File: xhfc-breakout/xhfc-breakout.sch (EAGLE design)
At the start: 2 parts, among them U1 XHFC-2SU

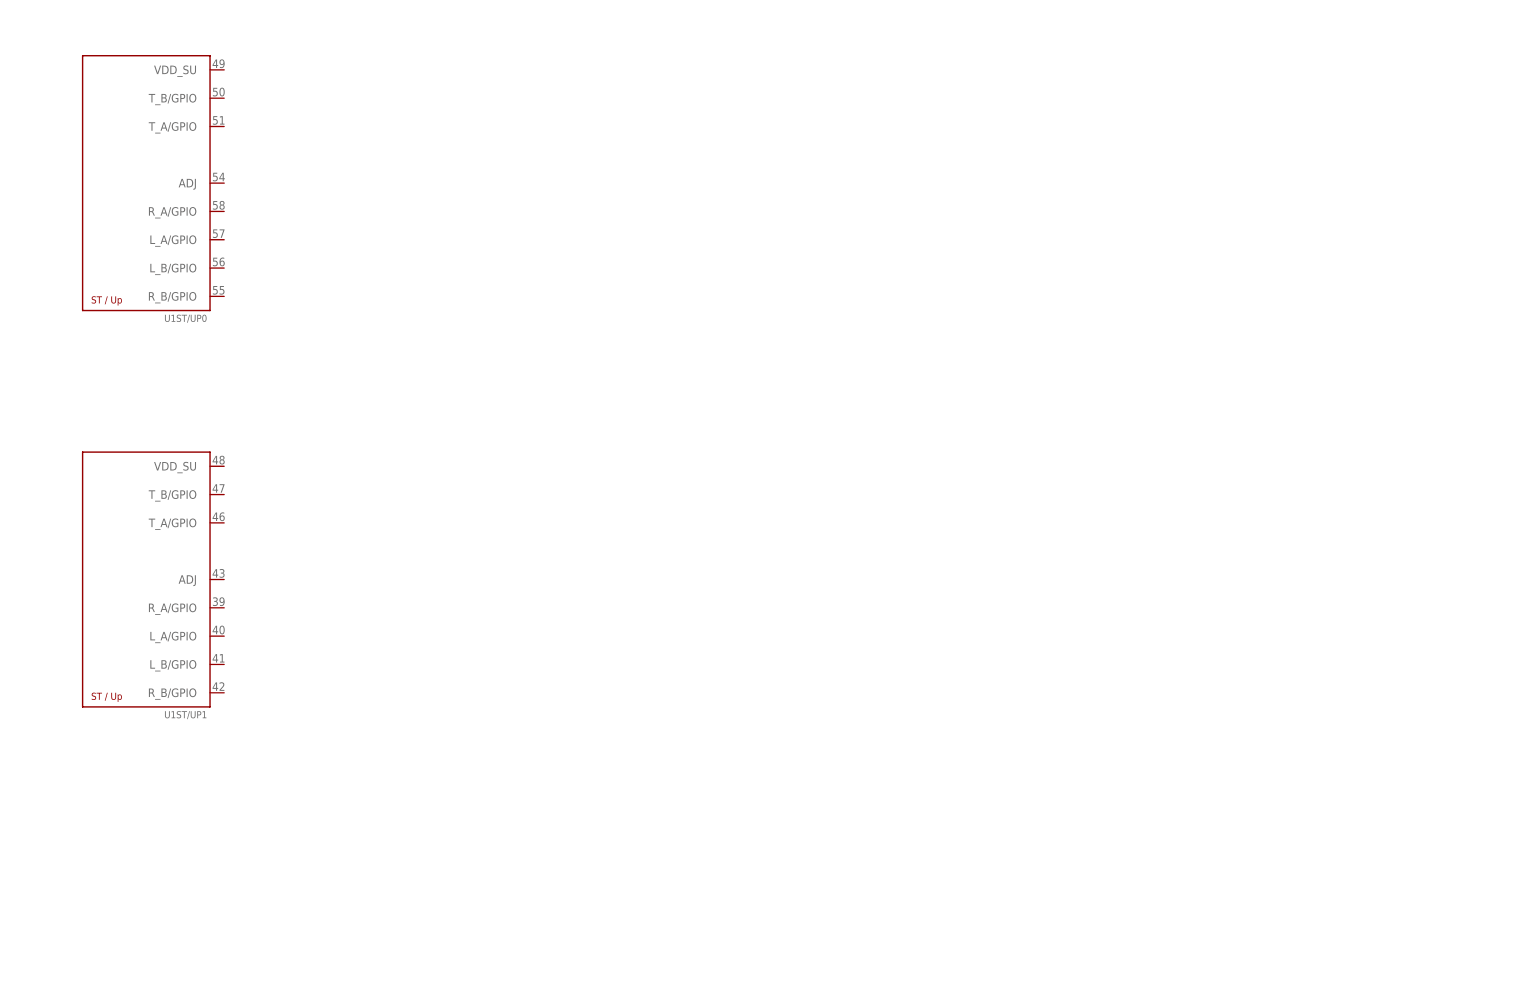
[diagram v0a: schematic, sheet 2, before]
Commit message: xhfc-breakout: Complete line interface from chip to RJ45
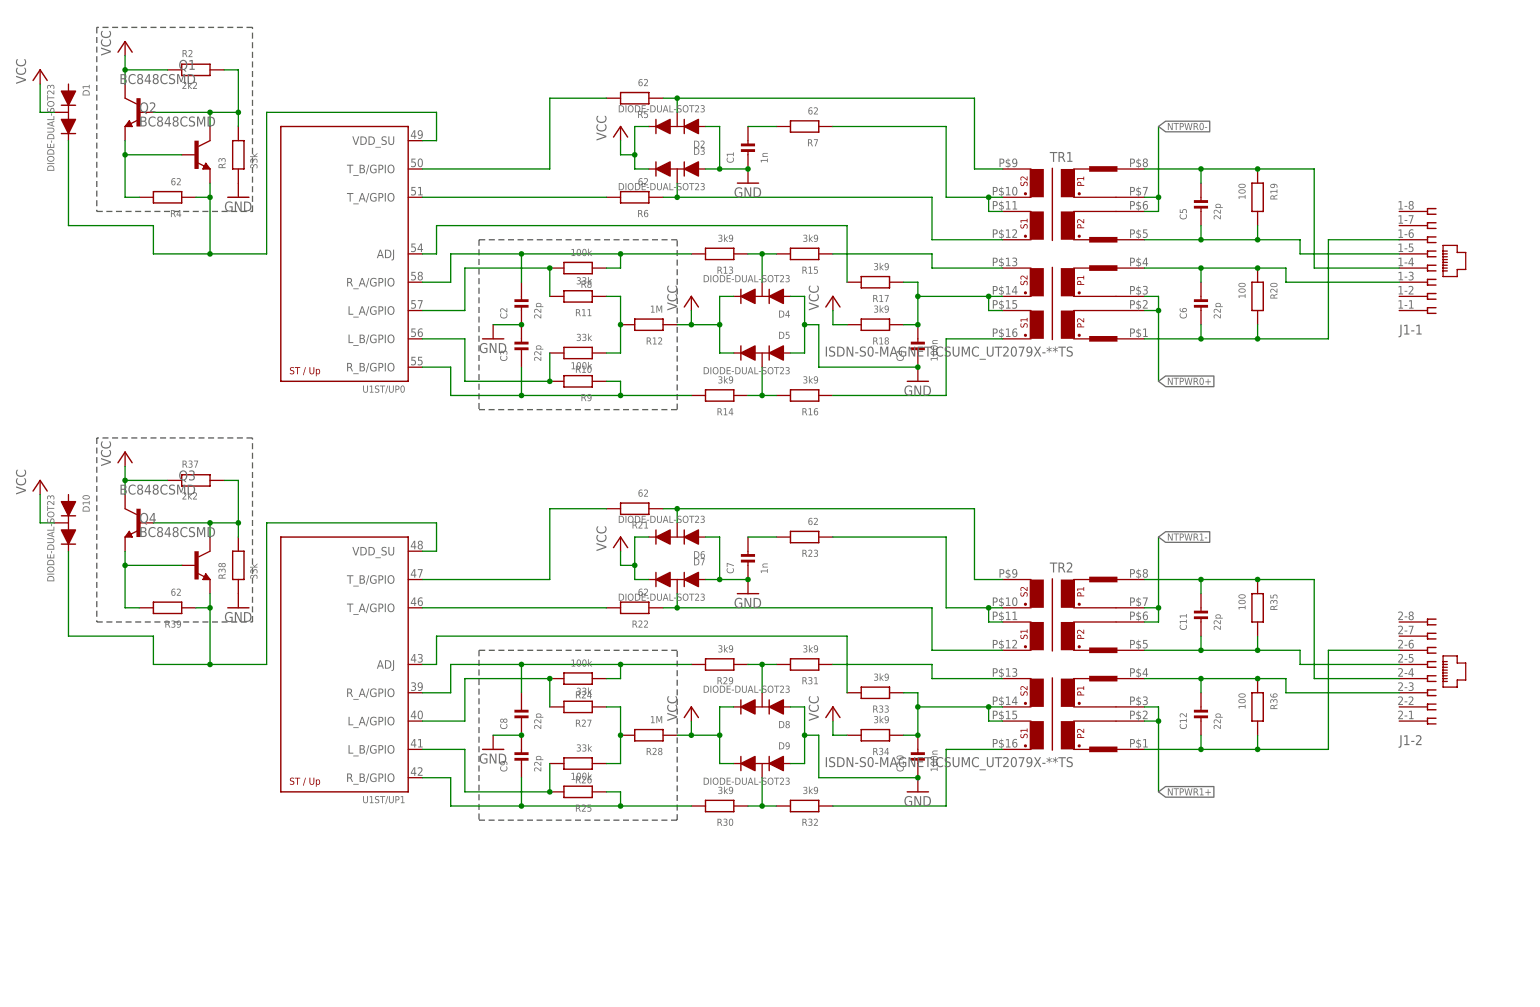
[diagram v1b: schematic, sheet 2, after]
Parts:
- added C1, C7: 1n, rc-sysmocom:CAP_CERAMIC_0603
- added C10, C4: 100n, rc-sysmocom:CAP_CERAMIC_0603
- added C11, C12, C2, C3, C5, C6, C8, C9: 22p, rc-sysmocom:CAP_CERAMIC_0603
- added D1, D10, D2, D3, D4, D5, D6, D7, D8, D9: DIODE-DUAL-SOT23, diodes-sysmocom:DIODE-DUAL-SOT23
- added J1: (no value), con-amp:557560-1
- added Q1, Q2, Q3, Q4: BC848CSMD, transistor-npn:BC848CSMD
- added R10, R11, R26, R27, R3, R38: 33k, rc-sysmocom:RESISTOR_0603
- added R12, R28: 1M, rc-sysmocom:RESISTOR_0603
- added R13, R14, R15, R16, R17, R18, R29, R30, R31, R32, R33, R34: 3k9, rc-sysmocom:RESISTOR_0603
- added R19, R20, R35, R36: 100, rc-sysmocom:RESISTOR_0603
- added R2, R37: 2k2, rc-sysmocom:RESISTOR_0603
- added R21, R22, R23, R39, R4, R5, R6, R7: 62, rc-sysmocom:RESISTOR_0603
- added R24, R25, R8, R9: 100k, rc-sysmocom:RESISTOR_0603
- added TR1, TR2: ISDN-S0-MAGNETICSUMC_UT2079X-**TS, isdn-magnetics:ISDN-S0-MAGNETICSUMC_UT2079X-**TS
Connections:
- new net N$1: Q1.B, Q2.C, R2.2, R3.2
- new net N$10: R7.1, TR1.10, TR1.11
- new net N$11: C3.1, R14.2, R9.1, U1ST/UP0.R_B/GPIO
- new net N$12: C2.2, R13.2, R8.1, U1ST/UP0.R_A/GPIO
- new net N$13: R11.2, R8.2, U1ST/UP0.L_A/GPIO
- new net N$14: R17.2, U1ST/UP0.ADJ
- new net N$15: R10.2, R9.2, U1ST/UP0.L_B/GPIO
- new net N$16: R10.1, R11.1, R12.2
- new net N$17: D6.M, R21.1, TR2.9
- new net N$18: C5.2, J1-1.4, R19.1, TR1.8
- new net N$19: D4.M, R13.1, R15.2
- new net N$2: R5.2, U1ST/UP0.T_B/GPIO
- new net N$20: D5.M, R14.1, R16.2
- new net N$21: C5.1, J1-1.5, R19.2, TR1.5
- new net N$22: R15.1, TR1.13
- new net N$23: R16.1, TR1.16
- new net N$24: C4.2, R17.1, R18.1, TR1.14, TR1.15
- new net N$25: C6.2, J1-1.3, R20.1, TR1.4
- new net N$26: C6.1, J1-1.6, R20.2, TR1.1
- new net N$27: D7.M, R22.1, TR2.12
- new net N$28: R21.2, U1ST/UP1.T_B/GPIO
- new net N$29: R22.2, U1ST/UP1.T_A/GPIO
- new net N$3: Q1.E, Q2.B, R4.2
- new net N$30: C7.2, R23.2
- new net N$31: R23.1, TR2.10, TR2.11
- new net N$32: R33.2, U1ST/UP1.ADJ
- new net N$33: C9.1, R25.1, R30.2, U1ST/UP1.R_B/GPIO
- new net N$34: C8.2, R24.1, R29.2, U1ST/UP1.R_A/GPIO
- new net N$35: R24.2, R27.2, U1ST/UP1.L_A/GPIO
- new net N$36: R25.2, R26.2, U1ST/UP1.L_B/GPIO
- new net N$37: R26.1, R27.1, R28.2
- new net N$38: D8.M, R29.1, R31.2
- new net N$39: D9.M, R30.1, R32.2
- new net N$4: D1.C, Q2.E, R4.1, U1ST/UP0.VDD_SU
- new net N$40: R31.1, TR2.13
- new net N$41: R32.1, TR2.16
- new net N$42: C10.2, R33.1, R34.1, TR2.14, TR2.15
- new net N$43: C11.2, J1-2.4, R35.1, TR2.8
- new net N$44: C11.1, J1-2.5, R35.2, TR2.5
- new net N$45: C12.2, J1-2.3, R36.1, TR2.4
- new net N$46: C12.1, J1-2.6, R36.2, TR2.1
- new net N$47: Q3.B, Q4.C, R37.2, R38.2
- new net N$48: Q3.E, Q4.B, R39.2
- new net N$49: D10.C, Q4.E, R39.1, U1ST/UP1.VDD_SU
- new net N$5: R6.2, U1ST/UP0.T_A/GPIO
- new net N$6: D2.M, R5.1, TR1.9
- new net N$7: D3.M, R6.1, TR1.12
- new net N$8: C1.1, C7.1, D2.A, D3.A, D6.A, D7.A
- new net N$9: C1.2, R7.2
- new net NTPWR0+: TR1.2, TR1.3
- new net NTPWR0-: TR1.6, TR1.7
- new net NTPWR1+: TR2.2, TR2.3
- new net NTPWR1-: TR2.6, TR2.7
- net GND: now also C10.1, C2.1, C3.2, C4.1, C8.1, C9.2, D4.A, D5.A, D8.A, D9.A, R3.1, R38.1
- net VCC: now also D1.M, D10.M, D2.C, D3.C, D4.C, D5.C, D6.C, D7.C, D8.C, D9.C, Q1.C, Q3.C, R12.1, R18.2, R2.1, R28.1, R34.2, R37.1
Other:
- moved on the sheet: U1ST/UP0, U1ST/UP1

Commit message: xhfc-breakout: Smash parts / align labels / better readability
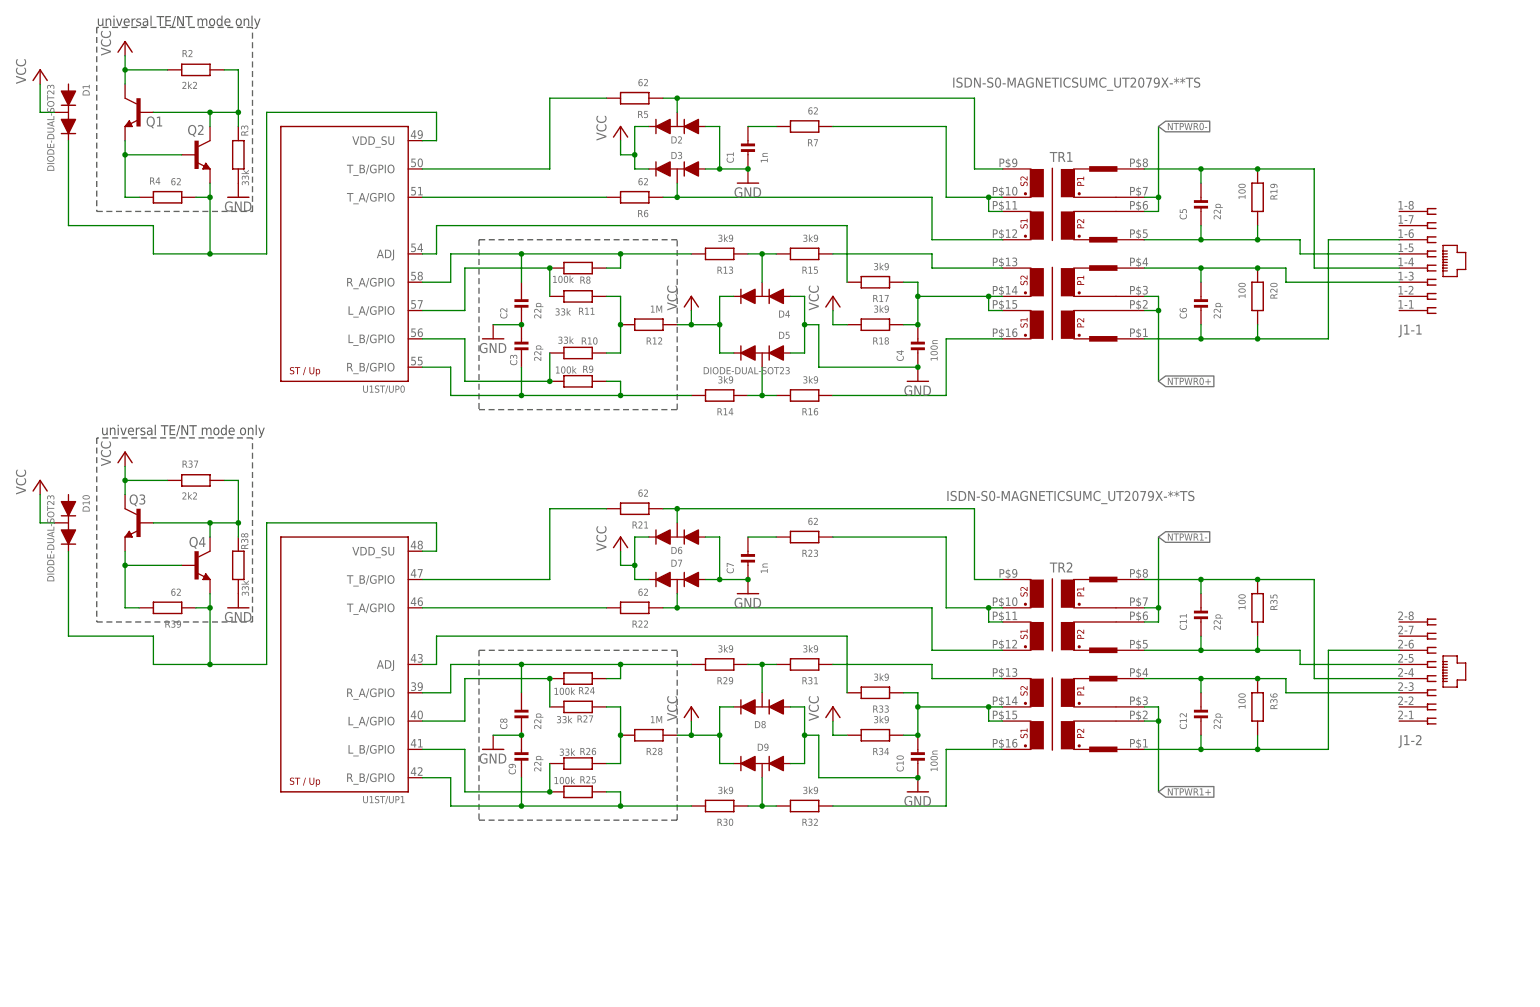
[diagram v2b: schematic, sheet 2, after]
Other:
- note added: "universal TE/NT mode only"

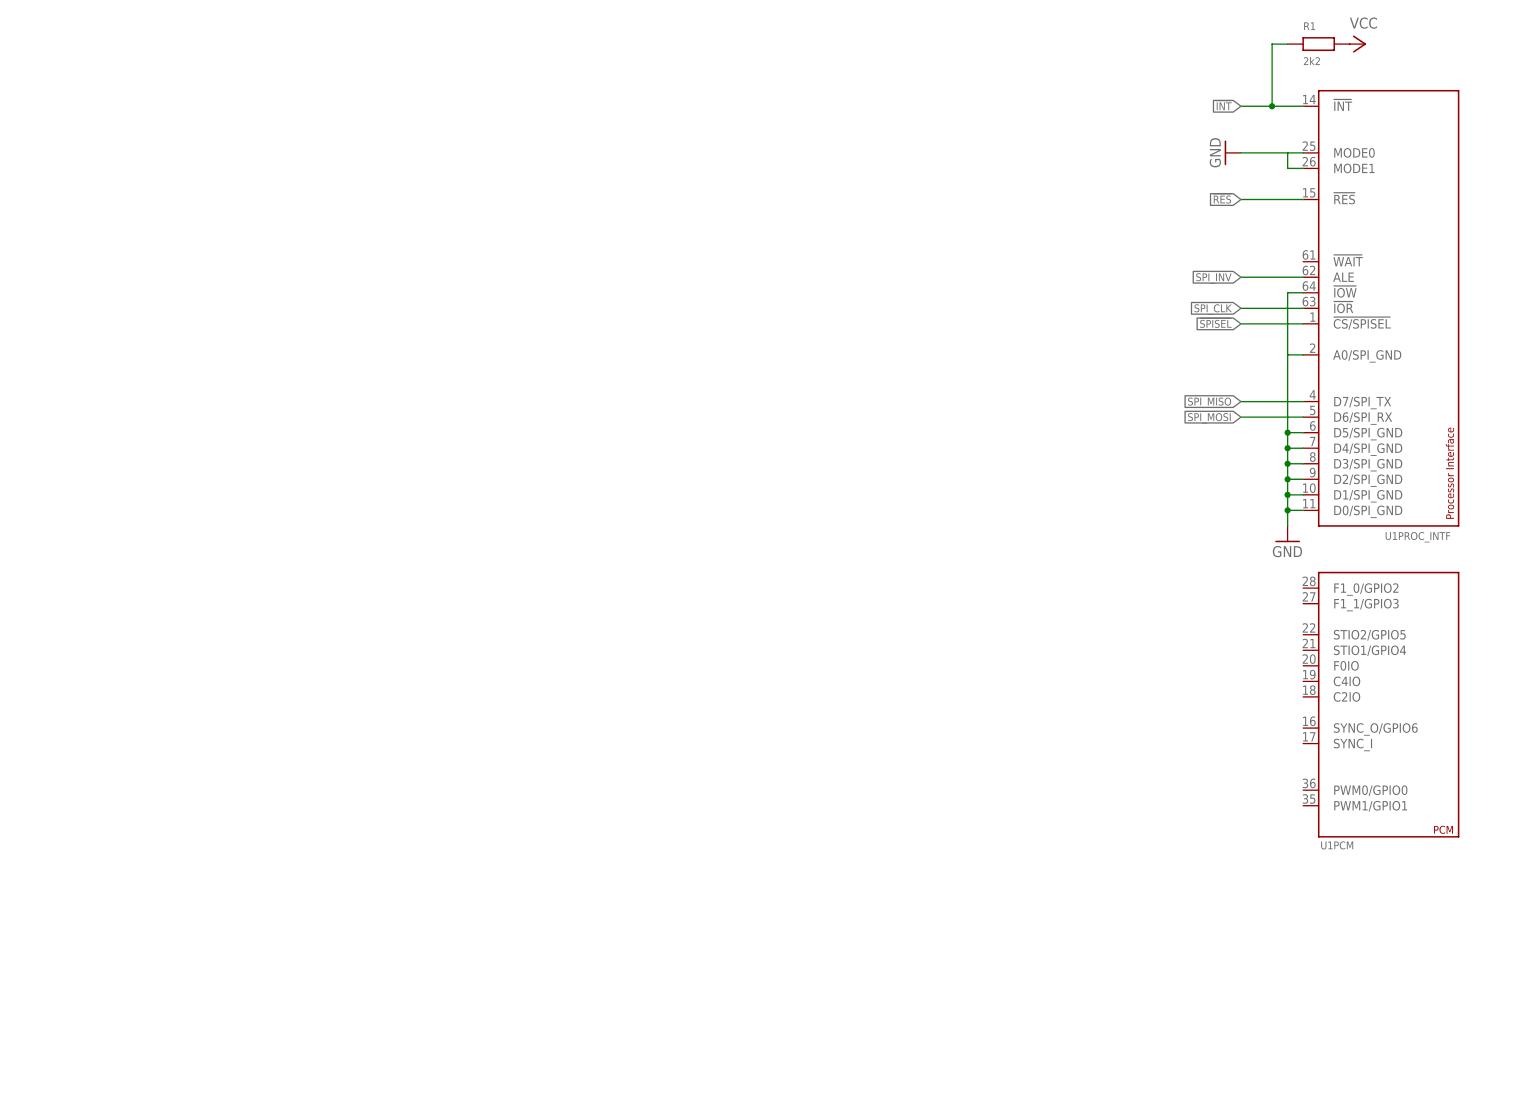
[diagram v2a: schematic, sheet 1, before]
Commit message: xhfc-breakout: partial PCB layout / component arrangement
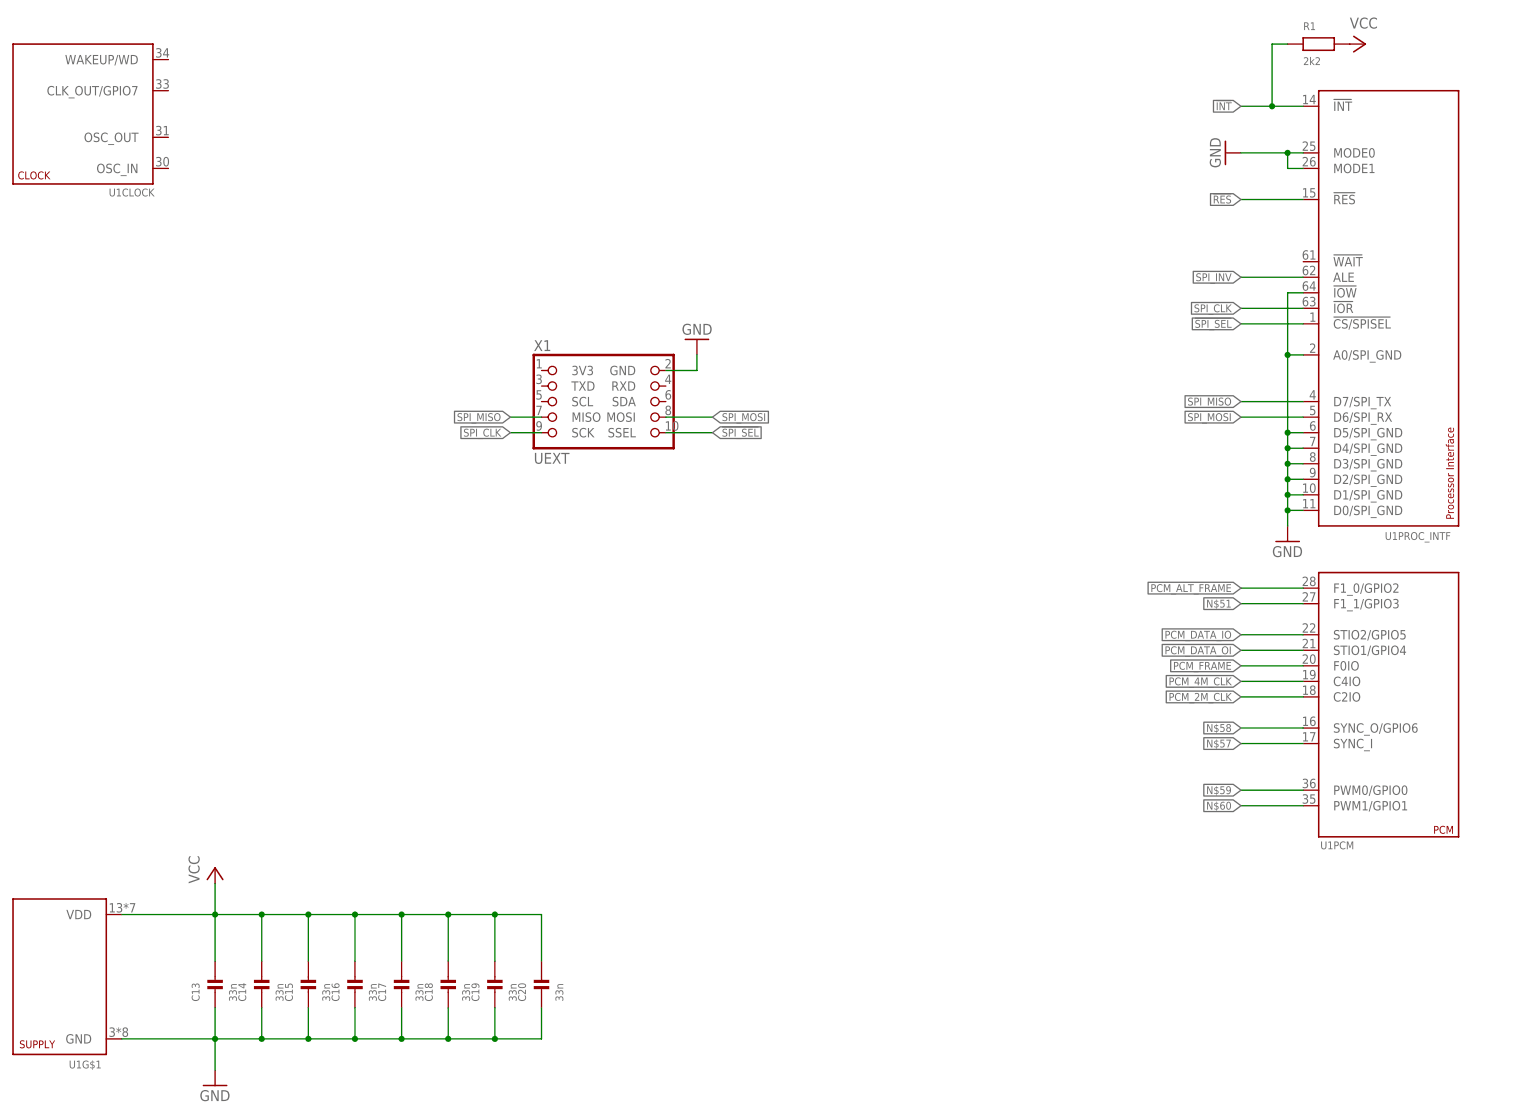
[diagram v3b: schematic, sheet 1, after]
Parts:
- added C13, C14, C15, C16, C17, C18, C19, C20: 33n, rc-sysmocom:CAP_CERAMIC_0603
- added X1: UEXT, laforge:UEXT
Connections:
- removed net !SPISEL: U1PROC_INTF.!CS/SPISEL
- removed net N$8: C1.1, C7.1, D2.A, D3.A, D6.A, D7.A
- new net !SPI_SEL: U1PROC_INTF.!CS/SPISEL, X1.SSEL
- new net N$51: U1PCM.F1_1/GPIO3
- new net N$57: U1PCM.SYNC_I
- new net N$58: U1PCM.SYNC_O/GPIO6
- new net N$59: U1PCM.PWM0/GPIO0
- new net N$60: U1PCM.PWM1/GPIO1
- new net PCM_2M_CLK: U1PCM.C2IO
- new net PCM_4M_CLK: U1PCM.C4IO
- new net PCM_ALT_FRAME: U1PCM.F1_0/GPIO2
- new net PCM_DATA_IO: U1PCM.STIO2/GPIO5
- new net PCM_DATA_OI: U1PCM.STIO1/GPIO4
- new net PCM_FRAME: U1PCM.F0IO
- net GND: now also C1.1, C13.1, C14.1, C15.1, C16.1, C17.1, C18.1, C19.1, C20.1, C7.1, D2.A, D3.A, D6.A, D7.A, U1G$1.GND, X1.GND
- net N$18: now also J1-2.5; no longer J1-1.4
- net N$21: now also J1-2.4; no longer J1-1.5
- net N$25: now also J1-2.6; no longer J1-1.3
- net N$26: now also J1-2.3; no longer J1-1.6
- net N$43: now also J1-1.4; no longer J1-2.4
- net N$44: now also J1-1.5; no longer J1-2.5
- net N$45: now also J1-1.3; no longer J1-2.3
- net N$46: now also J1-1.6; no longer J1-2.6
- net SPI_CLK: now also X1.SCK
- net SPI_MISO: now also X1.MISO
- net SPI_MOSI: now also X1.MOSI
- net VCC: now also C13.2, C14.2, C15.2, C16.2, C17.2, C18.2, C19.2, C20.2, U1G$1.VDD
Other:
- moved on the sheet: J1-1, J1-2
